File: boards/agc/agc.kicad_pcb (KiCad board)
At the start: 4 copper layers, 158.7 x 121.9 mm, 190 parts, among them J1 Conn_02x31_Top_Bottom, J2 Conn_01x24, J3 Conn_02x13_Top_Bottom, J4 Conn_01x24, Q1 MMBT2222, Q10 MMBT2222, Q11 MMBT2222, Q12 MMBT2222, Q13 MMBT2222, Q14 MMBT2222, Q15 MMBT2222, Q16 MMBT2222, Q17 MMBT2222, Q18 MMBT2222, Q19 MMBT2222, Q2 MMBT2222, Q20 MMBT2222, Q21 MMBT2222, Q22 MMBT2222, Q23 MMBT2222, Q24 MMBT2222, Q3 MMBT2222, Q4 MMBT2222, Q5 MMBT2222, Q6 MMBT2222, Q7 MMBT2222, Q8 MMBT2222, Q9 MMBT2222, T1 2:1, T10 2:1, T11 2:1, T12 2:1, T13 2:1, T14 2:1, T15 2:1, T16 2:1, T17 2:1, T18 2:1, T19 2:1, T2 2:1, T20 2:1, T21 2:1, T22 2:1, T23 2:1, T24 2:1, T25 2:1, T26 2:1, T3 2:1, T4 2:1, T5 2:1, T6 2:1, T7 2:1, T8 2:1, T9 2:1, U1 LM317L_SO8

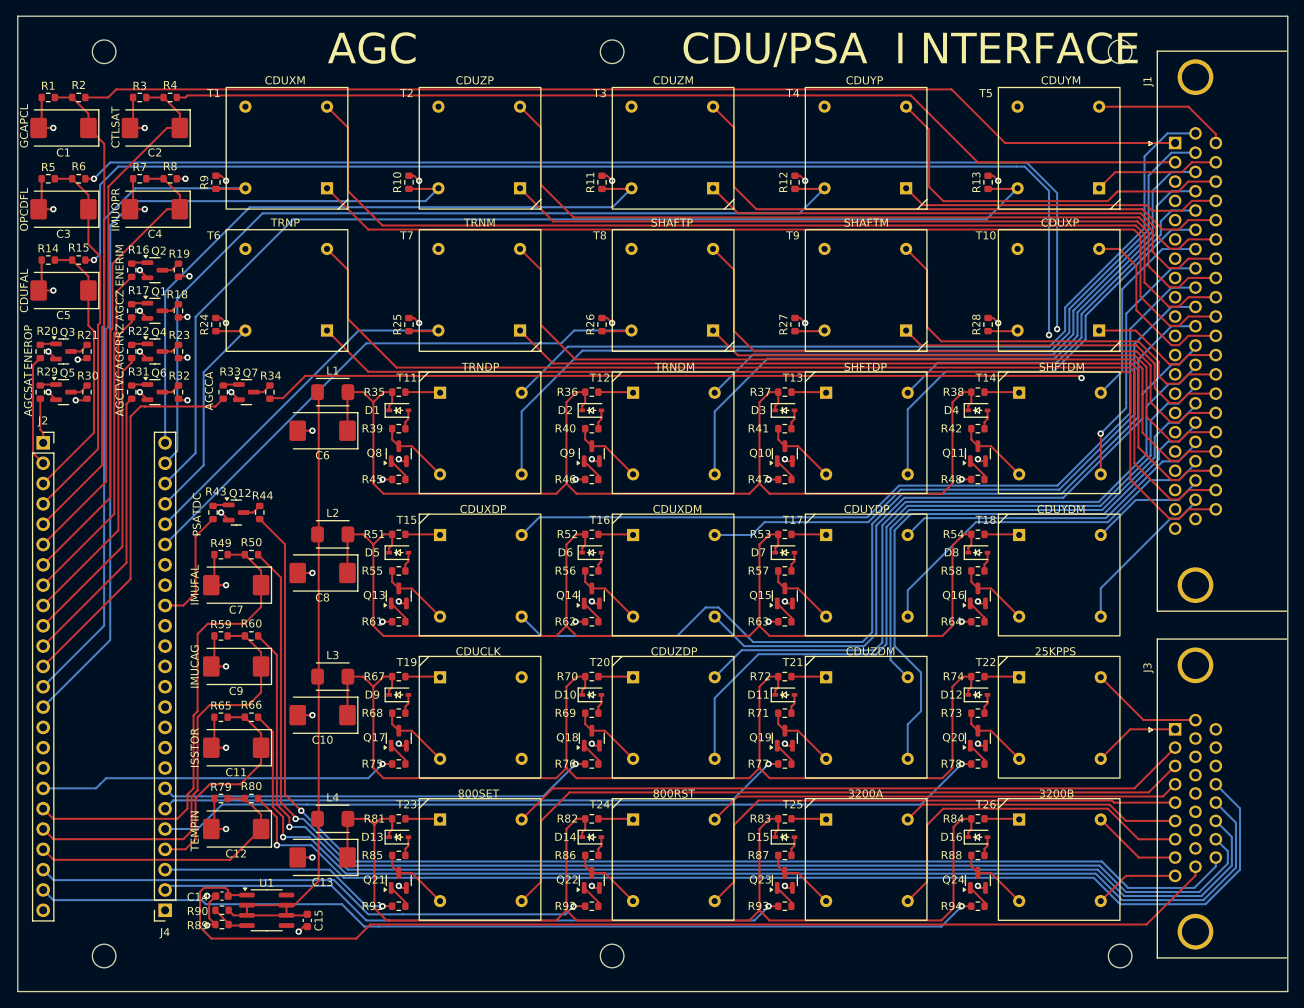
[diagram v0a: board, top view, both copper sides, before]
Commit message: Revised AGC board to include RRPONA, RD874, and 28V/14V analog sensing
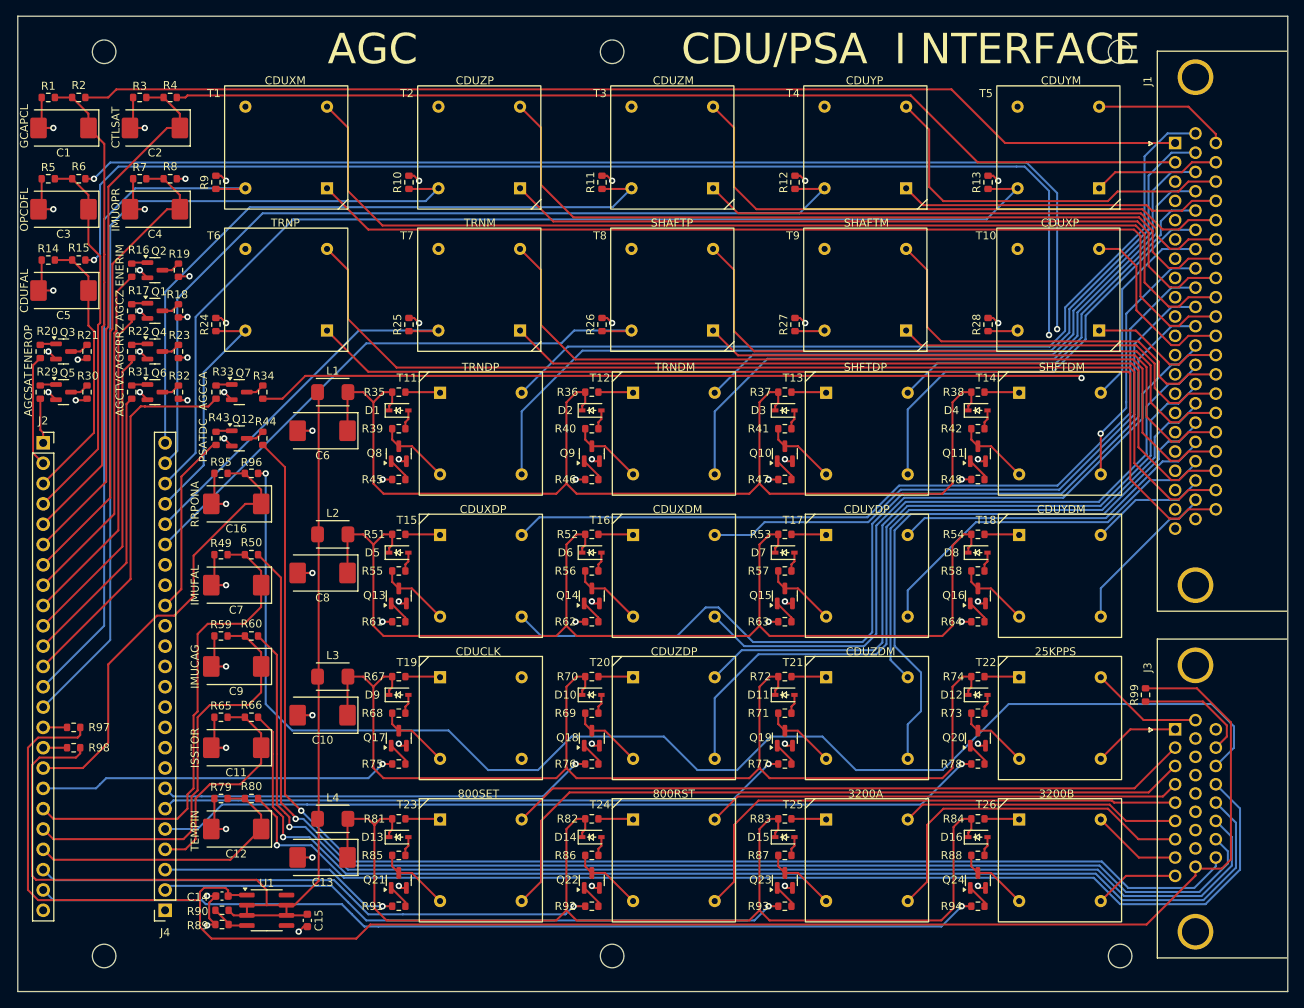
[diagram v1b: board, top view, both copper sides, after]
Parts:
- added C16: 6.8uF, Capacitor_Tantalum_SMD:CP_EIA-7343-31_Kemet-D, F.Cu at (128.3, 77.5)
- added R95: 2000, Resistor_SMD:R_0603_1608Metric, F.Cu at (126.4, 73.7)
- added R96: 20k, Resistor_SMD:R_0603_1608Metric, F.Cu at (130.2, 73.7)
- added R97: 30k, Resistor_SMD:R_0603_1608Metric, F.Cu at (108.0, 105.4)
- added R98: 13k, Resistor_SMD:R_0603_1608Metric, F.Cu at (108.0, 108.0)
- added R99: 2000, Resistor_SMD:R_0603_1608Metric, F.Cu at (241.9, 101.3)
- moved Q12 9.28 mm to (128.7, 69.3)
- moved R43 9.28 mm to (125.7, 69.3)
- moved R44 9.28 mm to (131.6, 69.3)
- moved R34 0.89 mm to (131.6, 63.5)
- moved R33 0.89 mm to (125.7, 63.5)
- moved Q7 0.89 mm to (128.7, 63.5)
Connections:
- J2 pad 15: unconnected-(J2-Pin_15-Pad15) -> Net-(J2-Pin_15)
- J2 pad 16: unconnected-(J2-Pin_16-Pad16) -> Net-(J2-Pin_16)
- J2 pad 17: unconnected-(J2-Pin_17-Pad17) -> /RRPONA
- J3 pad 20: unconnected-(J3-Pin_20-Pad20) -> /RD874
- J3 pad 21: unconnected-(J3-Pin_21-Pad21) -> /PSARRP
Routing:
- net /PSARRP: track 0.00 -> 171.6 mm, vias 0 -> 1
- net /+28V: track 140.8 -> 223.3 mm
- net /RRPONA: track 0.00 -> 56.4 mm
- net +14V: track 84.4 -> 137.6 mm
- net /RD874: track 0.00 -> 14.8 mm
- net /PSATDC: track 159.1 -> 168.3 mm
- net /ISSTDC: track 14.6 -> 22.9 mm
- net GND: track 110.3 -> 116.1 mm, vias 50 -> 51
- net Net-(J2-Pin_16): track 0.00 -> 2.98 mm
- net Net-(J2-Pin_15): track 0.00 -> 2.98 mm
- net /AGCCA: track 115.3 -> 116.2 mm
- net /COARSE: track 48.3 -> 47.4 mm
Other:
- board text added: "RRPONA"
